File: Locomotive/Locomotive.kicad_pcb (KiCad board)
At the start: 2 copper layers, 47.5 x 39.1 mm, 6 parts

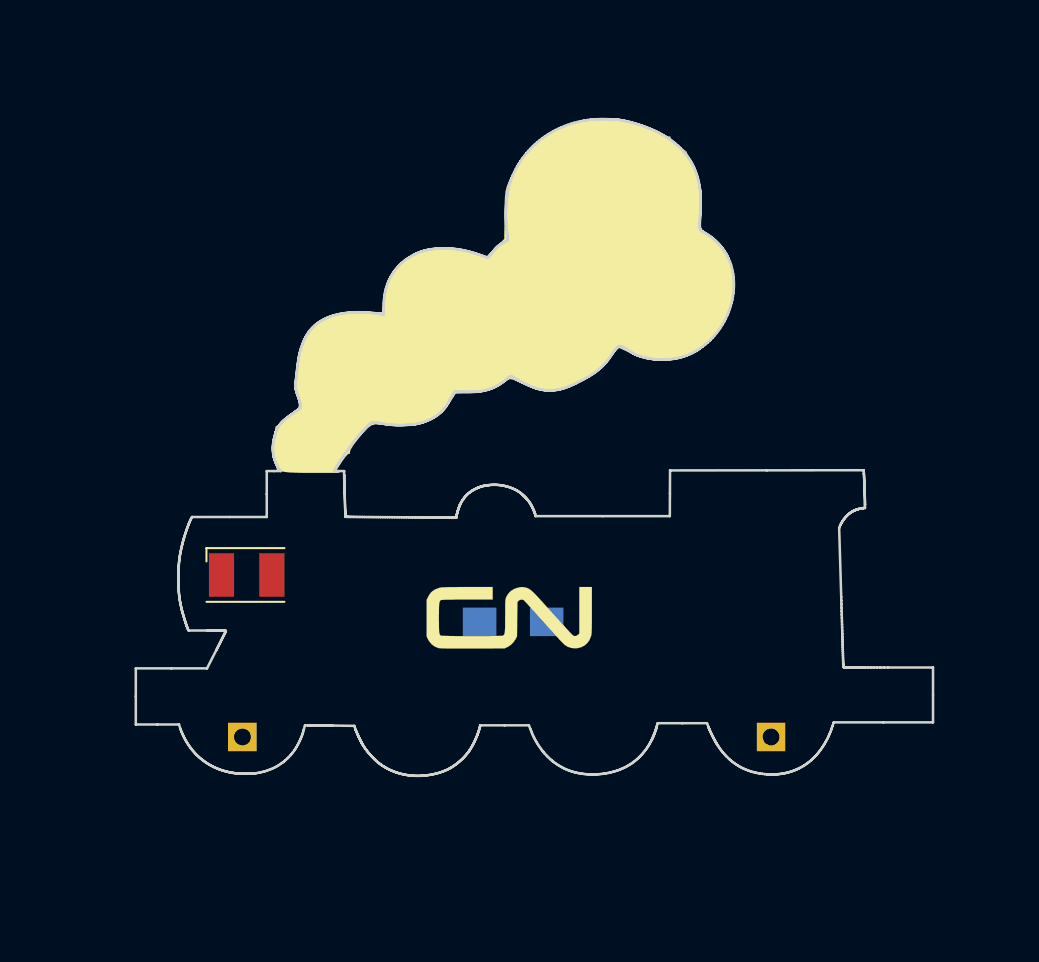
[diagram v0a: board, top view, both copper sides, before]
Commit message: Add & Align Pins
Add pins to all trains and set proper locations
Move RGB LEDs and resistors
Connect RGB LEDs to resistors and speaker to Arduino
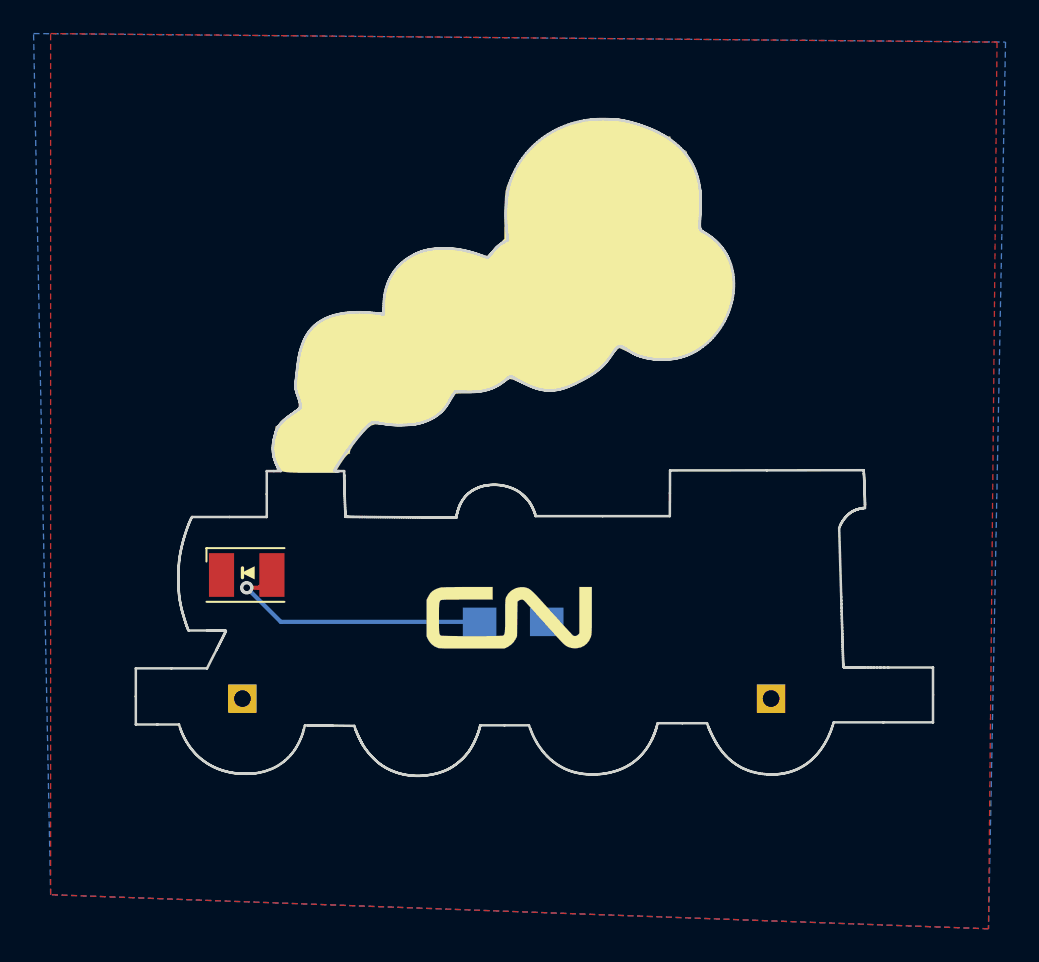
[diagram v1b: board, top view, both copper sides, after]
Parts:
- MK2: value 2 -> GND
- moved MK1 2.29 mm to (6.35, 39.1)
- moved MK2 2.29 mm to (37.8, 39.1)
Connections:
- net Net-(D1-Pad1) renamed /GND
- net Net-(MK1-Pad1) renamed /VCC
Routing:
- net Net-(D1-Pad2): track 0.00 -> 16.5 mm, vias 0 -> 1
- added copper zone on F.Cu, net /GND
- added copper zone on B.Cu, net /VCC
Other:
- board text added: "▲"
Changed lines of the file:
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@@
   (general
     (thickness 1.6)
-    (drawings 2876)
-    (tracks 0)
+    (drawings 2878)
+    (tracks 5)
     (zones 0)
     (modules 6)
@@
   (net 0 "")
   (net 1 "Net-(D1-Pad2)")
-  (net 2 "Net-(D1-Pad1)")
-  (net 3 "Net-(MK1-Pad1)")
+  (net 2 /GND)
+  (net 3 /VCC)
   (net_class Default "This is the default net class."
     (clearance 0.2)
@@
     (uvia_dia 0.3)
     (uvia_drill 0.1)
-    (add_net "Net-(D1-Pad1)")
+    (add_net /GND)
+    (add_net /VCC)
     (add_net "Net-(D1-Pad2)")
-    (add_net "Net-(MK1-Pad1)")
   )
   (module silkscreen:CN-Large (layer F.Cu)
@@
       (net 1 "Net-(D1-Pad2)"))
     (pad 1 smd rect (at -1.5 0) (size 1.5 2.6) (layers F.Cu F.Paste F.Mask)
-      (net 2 "Net-(D1-Pad1)"))
+      (net 2 /GND))
     (model ${KISYS3DMOD}/LEDs.3dshapes/LED_PLCC-2.wrl
       (at (xyz 0 0 0))
@@
   )
   (module Pin_Headers:Pin_Header_Angled_1x01_Pitch2.54mm (layer B.Cu)
-    (at 6.35 41.402 270)
+    (at 6.35 39.116 270)
     (descr "Through hole angled pin header, 1x01, 2.54mm pitch, 6mm pin length, single row")
     (tags "Through hole angled pin header THT 1x01 2.54mm single row")
-    (fp_text reference MK1 (at 4.385 2.27 270) (layer B.SilkS)
+    (fp_text reference MK1 (at 4.385 2.27 270) (layer B.Fab)
       (effects (font (size 1 1) (thickness 0.15)) (justify mirror))
     )
@@
     (fp_line (start 2.135 1.27) (end 4.04 1.27) (layer B.Fab) (width 0.1))
     (pad 1 thru_hole rect (at 0 0 270) (size 1.7 1.7) (drill 1) (layers *.Cu *.Mask)
-      (net 3 "Net-(MK1-Pad1)"))
+      (net 3 /VCC))
     (model ${KISYS3DMOD}/Pin_Headers.3dshapes/Pin_Header_Angled_1x01_Pitch2.54mm.wrl
       (at (xyz 0 0 0))
@@
   )
   (module Pin_Headers:Pin_Header_Angled_1x01_Pitch2.54mm (layer B.Cu)
-    (at 37.846 41.402 270)
+    (at 37.846 39.116 270)
     (descr "Through hole angled pin header, 1x01, 2.54mm pitch, 6mm pin length, single row")
     (tags "Through hole angled pin header THT 1x01 2.54mm single row")
-    (fp_text reference MK2 (at 4.385 2.27 270) (layer B.SilkS)
+    (fp_text reference MK2 (at 4.385 2.27 270) (layer B.Fab)
       (effects (font (size 1 1) (thickness 0.15)) (justify mirror))
     )
-    (fp_text value 2 (at 4.385 -2.27 270) (layer B.Fab)
+    (fp_text value GND (at 4.385 -2.27 270) (layer B.Fab)
       (effects (font (size 1 1) (thickness 0.15)) (justify mirror))
     )
@@
     )
     (pad 1 thru_hole rect (at 0 0 270) (size 1.7 1.7) (drill 1) (layers *.Cu *.Mask)
-      (net 2 "Net-(D1-Pad1)"))
+      (net 2 /GND))
     (model ${KISYS3DMOD}/Pin_Headers.3dshapes/Pin_Header_Angled_1x01_Pitch2.54mm.wrl
       (at (xyz 0 0 0))
@@
     )
     (pad 2 smd rect (at 2 0) (size 2 1.7) (layers B.Cu B.Paste B.Mask)
-      (net 3 "Net-(MK1-Pad1)"))
+      (net 3 /VCC))
     (pad 1 smd rect (at -2 0) (size 2 1.7) (layers B.Cu B.Paste B.Mask)
       (net 1 "Net-(D1-Pad2)"))
@@
     )
   )
+  (gr_line (start 6.35 31.33) (end 6.35 31.91) (layer F.SilkS) (width 0.2))
+  (gr_text ▲ (at 6.604 31.623 90) (layer F.SilkS)
+    (effects (font (size 0.75 0.75) (thickness 0.125)))
+  )
   (gr_line (start 16.350395 43.695886) (end 16.350453 43.695894) (layer Edge.Cuts) (width 0.15))
   (gr_line (start 20.516432 40.70908) (end 20.501789 40.778747) (layer Edge.Cuts) (width 0.15))
@@
   (gr_line (start 21.295605 12.460478) (end 21.315483 12.435317) (layer Edge.Cuts) (width 0.15))
   (gr_line (start 21.275604 12.486319) (end 21.295605 12.460478) (layer Edge.Cuts) (width 0.15))
+  (via (at 6.604 32.512) (size 0.8) (drill 0.4) (layers F.Cu B.Cu) (net 1))
+  (segment (start 8.636 34.544) (end 6.604 32.512) (width 0.25) (layer B.Cu) (net 1))
+  (segment (start 20.479 34.544) (end 8.636 34.544) (width 0.25) (layer B.Cu) (net 1))
+  (segment (start 7.342 32.512) (end 8.104 31.75) (width 0.25) (layer F.Cu) (net 1))
+  (segment (start 6.604 32.512) (end 7.342 32.512) (width 0.25) (layer F.Cu) (net 1))
+  (zone (net 2) (net_name /GND) (layer F.Cu) (hatch edge 0.508)
+    (connect_pads (clearance 0.508))
+    (min_thickness 0.254)
+    (fill yes (arc_segments 16) (thermal_gap 0.508) (thermal_bridge_width 0.508))
+    (polygon
+      (pts
+        (xy -5.08 -0.508) (xy 51.308 0) (xy 50.8 52.832) (xy -5.08 50.8)
+      )
+    )
+  )
+  (zone (net 3) (net_name /VCC) (layer B.Cu) (hatch edge 0.508)
+    (connect_pads (clearance 0.508))
+    (min_thickness 0.254)
+    (fill yes (arc_segments 16) (thermal_gap 0.508) (thermal_bridge_width 0.508))
+    (polygon
+      (pts
+        (xy -6.096 -0.508) (xy 51.816 0) (xy 50.8 52.832) (xy -5.08 50.8)
+      )
+    )
+  )
 )

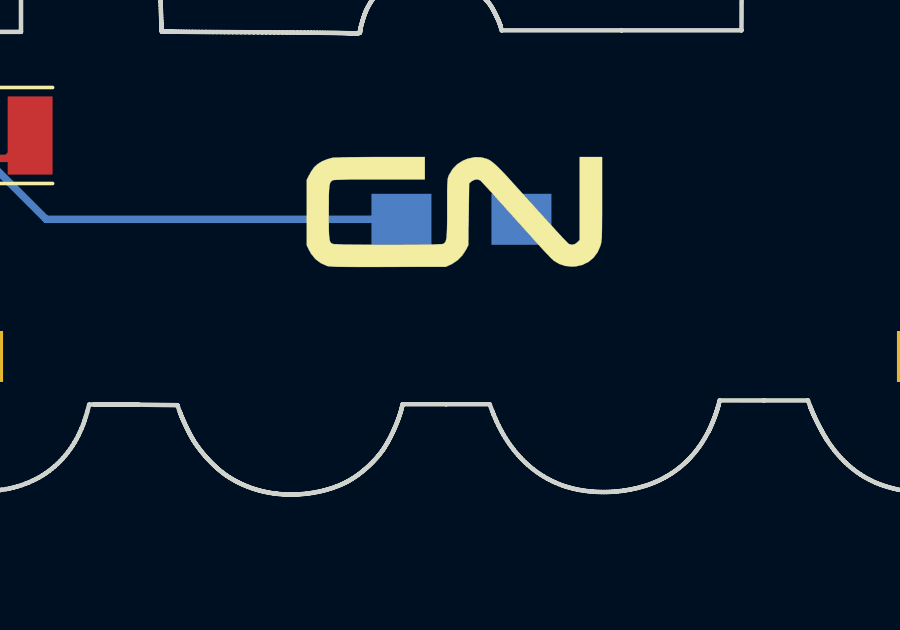
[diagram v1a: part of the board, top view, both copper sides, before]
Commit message: Finalize Tracks
Finish tracks for 3 RGB LEDs
Move date to locomotive, remove from caboose
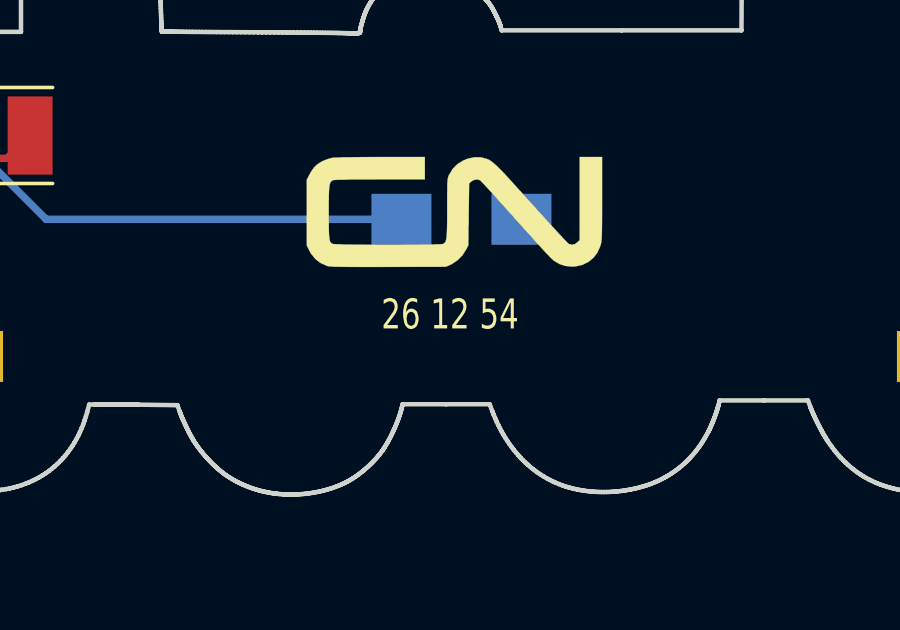
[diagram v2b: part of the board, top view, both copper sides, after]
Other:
- board text added: "26 12 54"
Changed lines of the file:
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@@
-(kicad_pcb (version 20171130) (host pcbnew 5.0.0-rc2-dev-unknown-bf135b0~64~ubuntu16.04.1)
+(kicad_pcb (version 20171130) (host pcbnew 5.0.0-rc2-dev-unknown-904eb82~65~ubuntu16.04.1)
   (general
     (thickness 1.6)
-    (drawings 2878)
+    (drawings 2879)
     (tracks 5)
     (zones 0)
@@
     )
   )
+  (gr_text "26 12 54" (at 22.098 37.719) (layer F.SilkS)
+    (effects (font (size 1 0.75) (thickness 0.1875)))
+  )
   (gr_line (start 6.35 31.33) (end 6.35 31.91) (layer F.SilkS) (width 0.2))

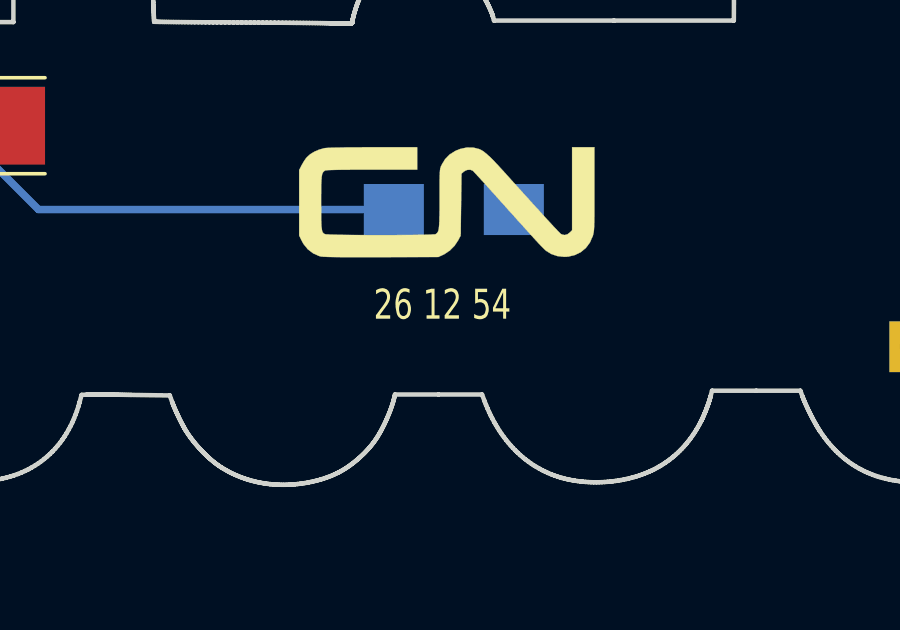
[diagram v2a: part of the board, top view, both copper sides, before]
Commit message: Update Text
Change dates on trains
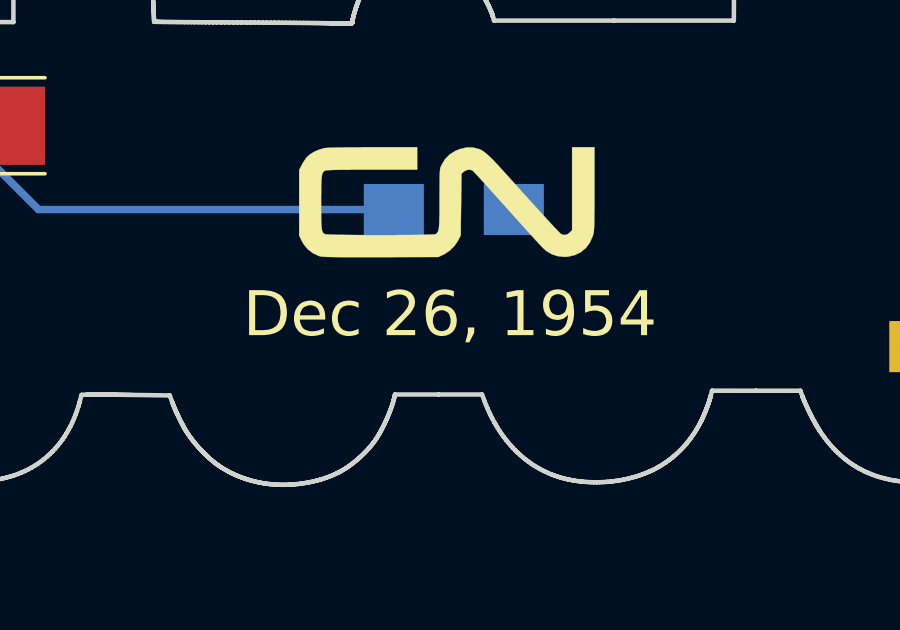
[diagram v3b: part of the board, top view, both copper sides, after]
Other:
- board text added: "150Ω"
- board text added: "Dec 26, 1954"
- board text removed: "26 12 54"
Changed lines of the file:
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@@
-(kicad_pcb (version 20171130) (host pcbnew 5.0.0-rc2-dev-unknown-904eb82~65~ubuntu16.04.1)
+(kicad_pcb (version 20171130) (host pcbnew 5.0.2-bee76a0~70~ubuntu18.04.1)
   (general
     (thickness 1.6)
-    (drawings 2879)
+    (drawings 2880)
     (tracks 5)
     (zones 0)
@@
     (pad_drill 0.762)
     (pad_to_mask_clearance 0.2)
+    (solder_mask_min_width 0.25)
     (aux_axis_origin 0 0)
     (visible_elements FFFFFF7F)
     (pcbplotparams
-      (layerselection 0x010fc_ffffffff)
-      (usegerberextensions false)
+      (layerselection 0x010f0_ffffffff)
+      (usegerberextensions true)
       (usegerberattributes false)
       (usegerberadvancedattributes false)
@@
       (hpglpennumber 1)
       (hpglpenspeed 20)
-      (hpglpendiameter 15)
+      (hpglpendiameter 15.000000)
       (psnegative false)
       (psa4output false)
@@
       (outputformat 1)
       (mirror false)
-      (drillshape 1)
+      (drillshape 0)
       (scaleselection 1)
-      (outputdirectory ""))
+      (outputdirectory "GERBER/"))
   )
   (net 0 "")
@@
     )
   )
-  (gr_text "26 12 54" (at 22.098 37.719) (layer F.SilkS)
-    (effects (font (size 1 0.75) (thickness 0.1875)))
+  (gr_text 150Ω (at 22.225 32.131) (layer B.SilkS)
+    (effects (font (size 1 1) (thickness 0.25)) (justify mirror))
+  )
+  (gr_text "Dec 26, 1954" (at 22.352 38.0365) (layer F.SilkS)
+    (effects (font (size 1.5 1.5) (thickness 0.375)))
   )
   (gr_line (start 6.35 31.33) (end 6.35 31.91) (layer F.SilkS) (width 0.2))
